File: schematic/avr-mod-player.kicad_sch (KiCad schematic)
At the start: 43 parts, among them J1 USBasp header, J2 DC-005 Power Jack, J3 RCA AV2-8.4-45, J4 Conn_02x04_Counter_Clockwise, U1 ATmega32A-P, U2 AM29F040B-90PC, U3 74HC595, U4 MCP6022, U5 L7805, Y1 16 MHz

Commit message: Schematic updated
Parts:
- R10, R7, R8, R9: value 470R -> 10k
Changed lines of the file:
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@@
 			)
 		)
-		(property "Value" "470R"
+		(property "Value" "10k"
 			(at 137.16 151.13 90)
 			(effects
@@
 			)
 		)
-		(property "Value" "470R"
+		(property "Value" "10k"
 			(at 137.16 173.99 90)
 			(effects
@@
 			)
 		)
-		(property "Value" "470R"
+		(property "Value" "10k"
 			(at 137.16 162.56 90)
 			(effects
@@
 			)
 		)
-		(property "Value" "470R"
+		(property "Value" "10k"
 			(at 137.16 185.42 90)
 			(effects

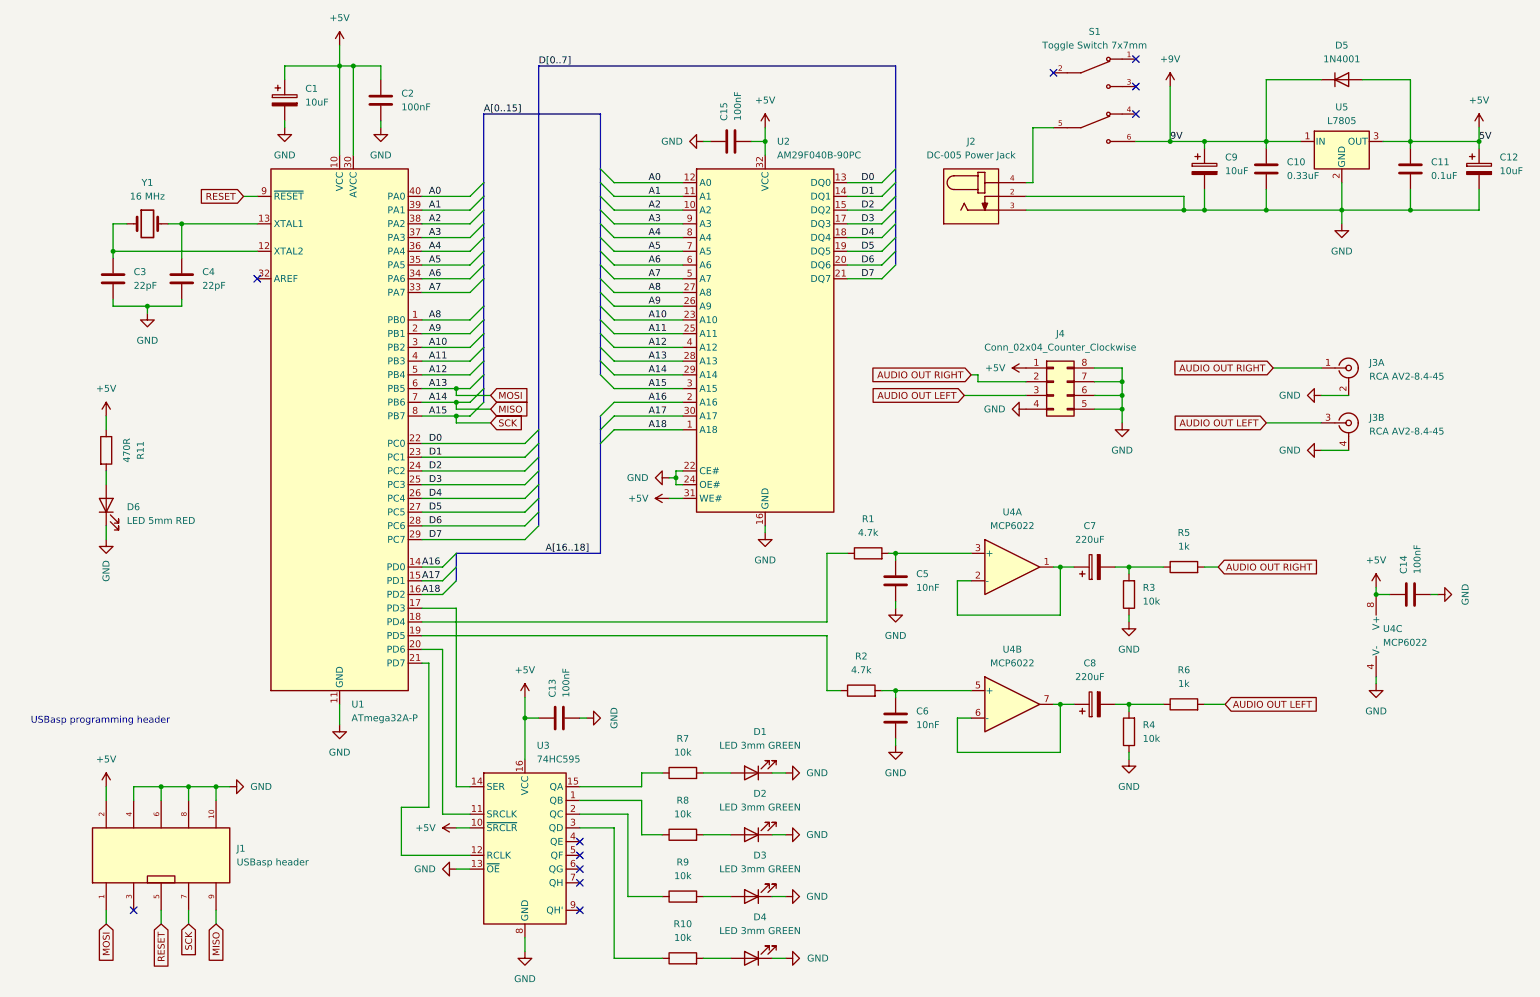
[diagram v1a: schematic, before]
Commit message: PCB added to schematic folder
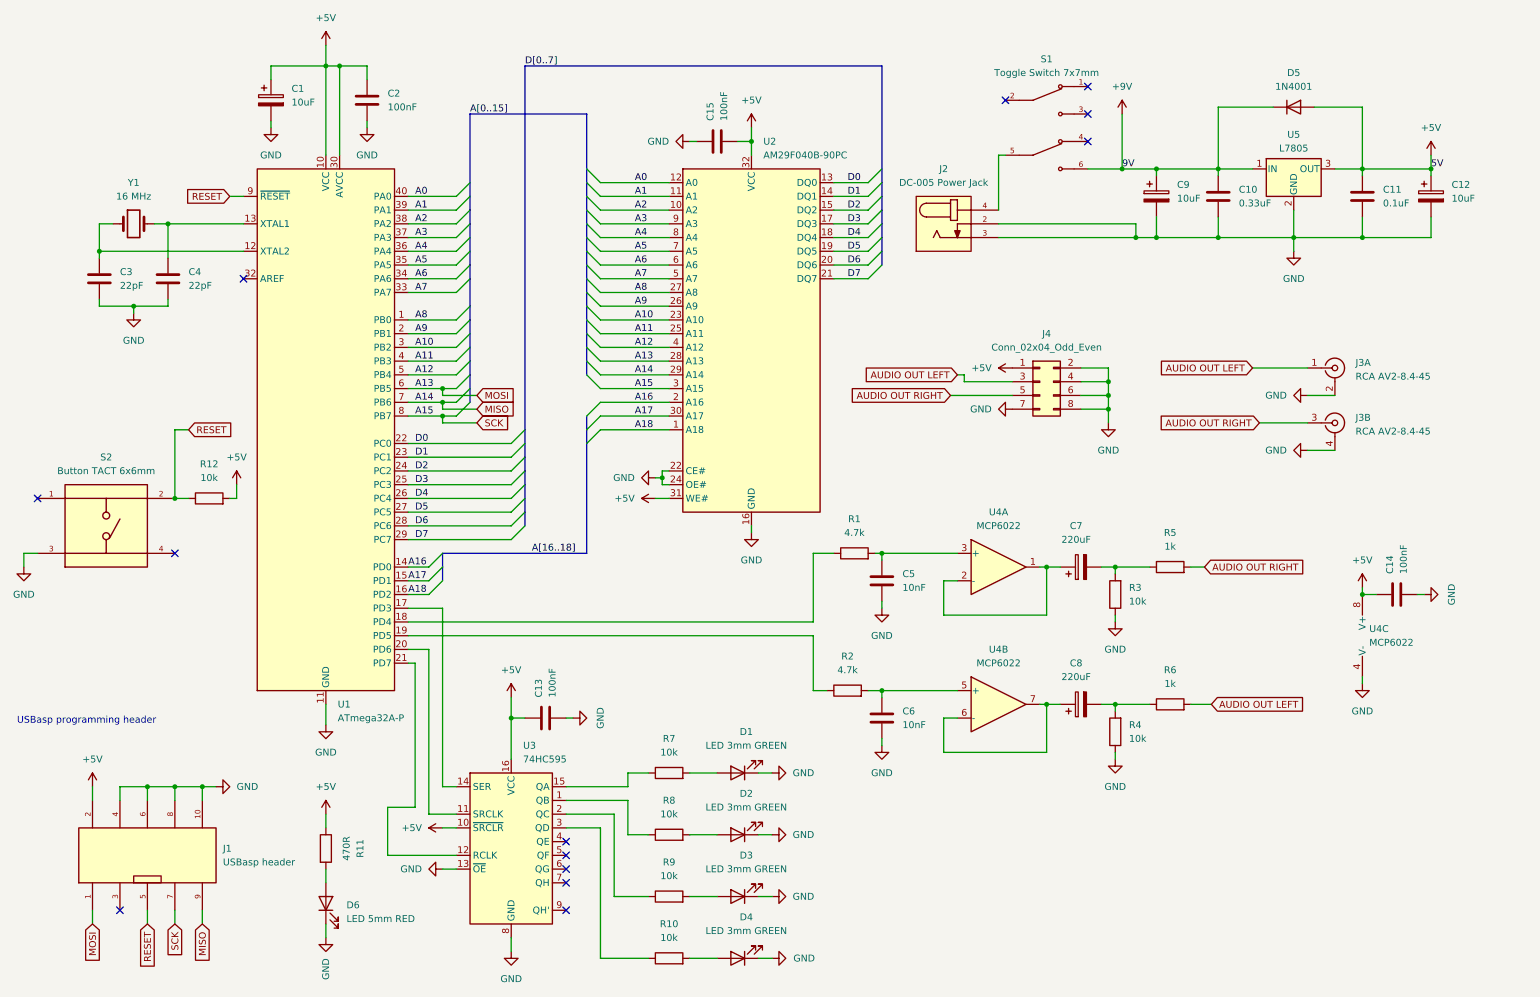
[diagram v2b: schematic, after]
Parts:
- added R12: 10k, StockLib:R_10k_Axial_DIN0207, symbol StockLib:R_10k
- added S2: Button TACT 6x6mm, StockLib:Button TACT 6x6mm, symbol StockLib:Button TACT 6x6mm
- J4: value Conn_02x04_Counter_Clockwise -> Conn_02x04_Odd_Even; footprint Connector_PinHeader_2.54mm:PinHeader_2x04_P2.54mm_Vertical -> Connector_PinSocket_2.54mm:PinSocket_2x04_P2.54mm_Vertical; symbol Connector_Generic:Conn_02x04_Counter_Clockwise -> Connector_Generic:Conn_02x04_Odd_Even
- U4: footprint (none) -> Package_DIP:DIP-8_W7.62mm
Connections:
- net +5V: now also R12.2
- net AUDIO OUT LEFT: now also J3.1 (In1); no longer J3.3 (In2)
- net AUDIO OUT RIGHT: now also J3.3 (In2), J4.5 (Pin_5); no longer J3.1 (In1), J4.2 (Pin_2)
- net GND: now also J4.2 (Pin_2), S2.3; no longer J4.5 (Pin_5)
- net RESET: now also R12.1, S2.2
- no-connect marks 11 -> 13
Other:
- moved on the sheet: C1, C10, C11, C12, C13, C14, C15, C2, C3, C4, C5, C6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

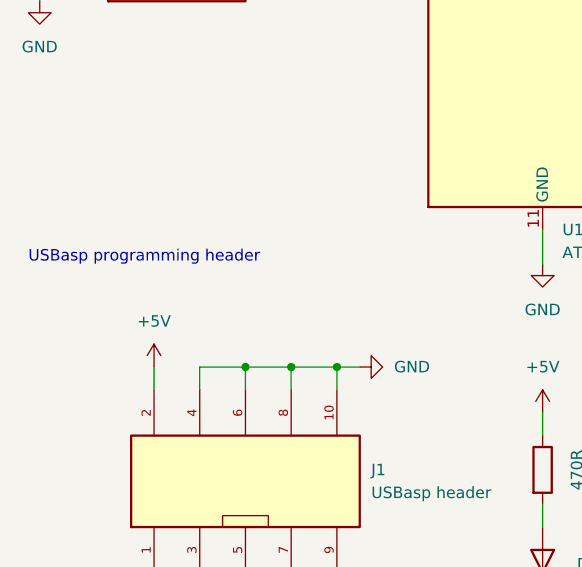
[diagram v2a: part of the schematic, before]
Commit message: Schottky diode added to ISP header for protection
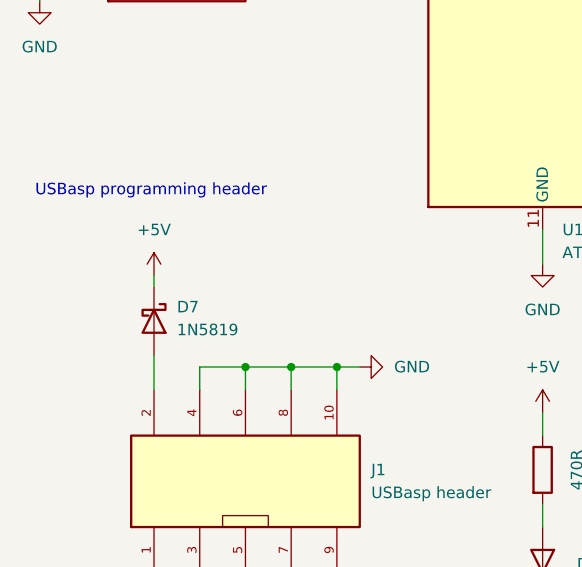
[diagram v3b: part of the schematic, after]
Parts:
- added D7: 1N5819, Diode_THT:D_DO-41_SOD81_P10.16mm_Horizontal, symbol StockLib:1N5819
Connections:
- net +5V: now also D7.1 (K); no longer J1.2
- new net: D7.2 (A), J1.2
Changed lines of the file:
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@@
 	(text "USBasp programming header"
 		(exclude_from_sim no)
-		(at 13.97 146.05 0)
+		(at 14.732 138.684 0)
 		(effects
 			(font
@@
 	(wire
 		(pts
-			(xy 27.94 157.48) (xy 27.94 160.02)
-		)
-		(stroke
-			(width 0)
-			(type default)
-		)
-	)
-	(wire
-		(pts
 			(xy 38.1 180.34) (xy 38.1 182.88)
 		)
@@
 		)
 	)
+	(wire
+		(pts
+			(xy 27.94 147.32) (xy 27.94 148.59)
+		)
+		(stroke
+			(width 0)
+			(type default)
+		)
+	)
 	(bus
 		(pts
@@
 	(wire
 		(pts
+			(xy 27.94 156.21) (xy 27.94 160.02)
+		)
+		(stroke
+			(width 0)
+			(type default)
+		)
+	)
+	(wire
+		(pts
 			(xy 86.36 104.14) (xy 105.41 104.14)
 		)
@@
 	(symbol
 		(lib_id "power:+5V")
-		(at 27.94 157.48 0)
+		(at 27.94 147.32 0)
 		(unit 1)
 		(exclude_from_sim no)
@@
 		(fields_autoplaced yes)
 		(property "Reference" "#PWR07"
-			(at 27.94 161.29 0)
+			(at 27.94 151.13 0)
 			(effects
 				(font
@@
 		)
 		(property "Value" "+5V"
-			(at 27.94 152.4 0)
+			(at 27.94 142.24 0)
 			(effects
 				(font
@@
 		)
 		(property "Footprint" ""
-			(at 27.94 157.48 0)
+			(at 27.94 147.32 0)
 			(effects
 				(font
@@
 		)
 		(property "Datasheet" ""
-			(at 27.94 157.48 0)
+			(at 27.94 147.32 0)
 			(effects
 				(font
@@
 		)
 		(property "Description" ""
-			(at 27.94 157.48 0)
+			(at 27.94 147.32 0)
 			(effects
 				(font
@@
 					(unit 1)
 				)
+			)
+		)
+	)
+	(symbol
+		(lib_id "StockLib:1N5819")
+		(at 27.94 152.4 270)
+		(unit 1)
+		(exclude_from_sim no)
+		(in_bom yes)
+		(on_board yes)
+		(dnp no)
+		(fields_autoplaced yes)
+		(property "Reference" "D7"
+			(at 30.48 150.8124 90)
+			(effects
+				(font
+					(size 1.27 1.27)
+				)
+				(justify left)
+			)
+		)
+		(property "Value" "1N5819"
+			(at 30.48 153.3524 90)
+			(effects
+				(font
+					(size 1.27 1.27)
+				)
+				(justify left)
+			)
+		)
+		(property "Footprint" "Diode_THT:D_DO-41_SOD81_P10.16mm_Horizontal"
+			(at 23.495 152.4 0)
+			(effects
+				(font
+					(size 1.27 1.27)
+				)
+				(hide yes)
+			)
+		)
+		(property "Datasheet" "http://www.vishay.com/docs/88525/1n5817.pdf"
+			(at 27.94 152.4 0)
+			(effects
+				(font
+					(size 1.27 1.27)
+				)
+				(hide yes)
+			)
+		)
+		(property "Description" "40V 1A Schottky Barrier Rectifier Diode, DO-41"
+			(at 27.94 152.4 0)
+			(effects
+				(font
+					(size 1.27 1.27)
+				)
+				(hide yes)
+			)
+		)
+		(pin "2"
+		)
+		(pin "1"
+		)
+		(instances
+			(project ""
+				(path "/ddc08fb2-4e50-46d6-b134-b09428b2126c"
+					(reference "D7")
+					(unit 1)
+				)
